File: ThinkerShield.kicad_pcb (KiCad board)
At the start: 2 copper layers, 69 x 69 mm, 41 parts, among them SW1 SW_PUSHBUTTON, SW2 SW_PUSHBUTTON, U1 BUZZER

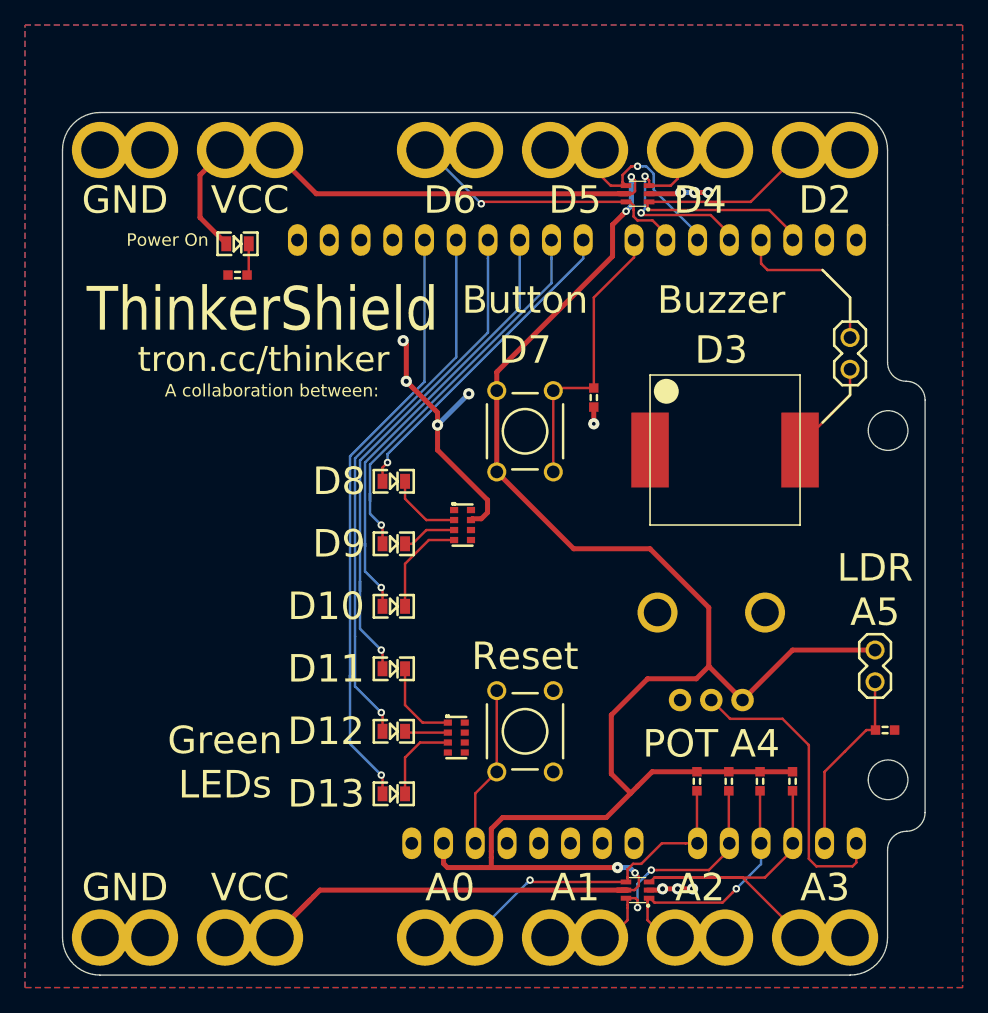
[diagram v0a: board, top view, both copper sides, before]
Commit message: Split resistor packs into individual resistors, spread LEDs out some more
Also includes upgrade to KiCad 2015-08 which no longer uses .cmp files
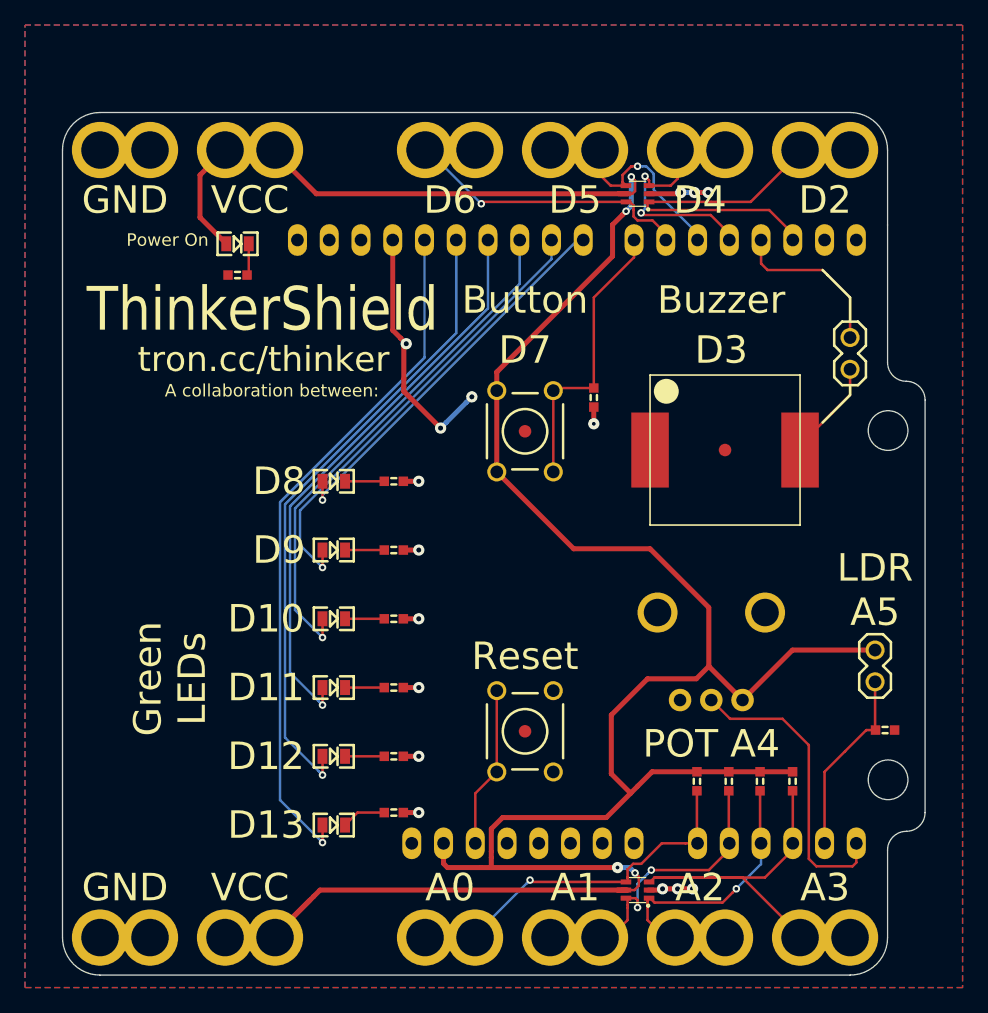
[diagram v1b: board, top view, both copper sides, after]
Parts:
- added FIDUCIAL: val**, FT:FIDUCIAL, F.Cu at (221.0, 71.0)
- added FIDUCIAL: val**, FT:FIDUCIAL, F.Cu at (205.0, 69.5)
- added FIDUCIAL: val**, FT:FIDUCIAL, F.Cu at (205.0, 93.5)
- added R10: 470R, FT:0603, F.Cu at (194.5, 84.5)
- added R11: 470R, FT:0603, F.Cu at (194.5, 90.0)
- added R12: 470R, FT:0603, F.Cu at (194.5, 95.5)
- added R13: 470R, FT:0603, F.Cu at (194.5, 100.0)
- R3, R4: footprint FT:RES_CAY16 -> FT:0603
- moved R4 15.8 mm to (194.5, 79.0), turned to 180 degrees
- moved R3 6.52 mm to (194.5, 73.5), turned to 180 degrees
- moved LED6 5.41 mm to (189.7, 101.0)
- moved LED5 5.20 mm to (189.7, 95.5)
- moved LED4 5.03 mm to (189.7, 90.0)
- moved LED3 4.90 mm to (189.7, 84.5)
- moved LED2 4.83 mm to (189.7, 79.0)
- moved LED1 4.80 mm to (189.7, 73.5)
- moved G*** 2.50 mm to (176.0, 74.0)
- moved LOGO_FREETRONICS 1.70 mm to (188.8, 69.5)
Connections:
- R3 pad 1: (no net) -> GND
- R3 pad 2: (no net) -> Net-(LED1-PadK)
- R4 pad 1: Net-(LED4-PadK) -> GND
- R4 pad 2: GND -> Net-(LED2-PadK)
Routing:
- net /D12: track 43.6 -> 51.2 mm
- net /D13: track 49.2 -> 56.7 mm
- net /D10: track 36.6 -> 43.0 mm
- net GND: track 39.4 -> 45.6 mm, vias 11 -> 16
- net /D11: track 42.7 -> 48.8 mm
- net /D9: track 31.3 -> 36.7 mm
- net /D8: track 27.4 -> 32.7 mm
- net Net-(LED3-PadK): track 8.21 -> 3.14 mm
- net Net-(LED4-PadK): track 6.91 -> 3.14 mm
- net Net-(LED6-PadK): track 6.82 -> 3.55 mm
- net Net-(LED1-PadK): track 6.03 -> 3.14 mm
- net Net-(LED2-PadK): track 4.38 -> 3.14 mm
